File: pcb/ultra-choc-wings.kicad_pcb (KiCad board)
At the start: 2 copper layers, 103.7 x 91.1 mm, 84 parts, among them Q1 AO3400A, SW1 CPG1316S01D02_reversible, SW10 CPG1316S01D02_reversible, SW11 CPG1316S01D02_reversible, SW12 CPG1316S01D02_reversible, SW13 CPG1316S01D02_reversible, SW14 CPG1316S01D02_reversible, SW15 CPG1316S01D02_reversible, SW16 CPG1316S01D02_reversible, SW17 CPG1316S01D02_reversible, SW18 CPG1316S01D02_reversible, SW2 CPG1316S01D02_reversible, SW3 CPG1316S01D02_reversible, SW4 CPG1316S01D02_reversible, SW5 CPG1316S01D02_reversible, SW6 CPG1316S01D02_reversible, SW7 CPG1316S01D02_reversible, SW8 CPG1316S01D02_reversible, SW9 CPG1316S01D02_reversible

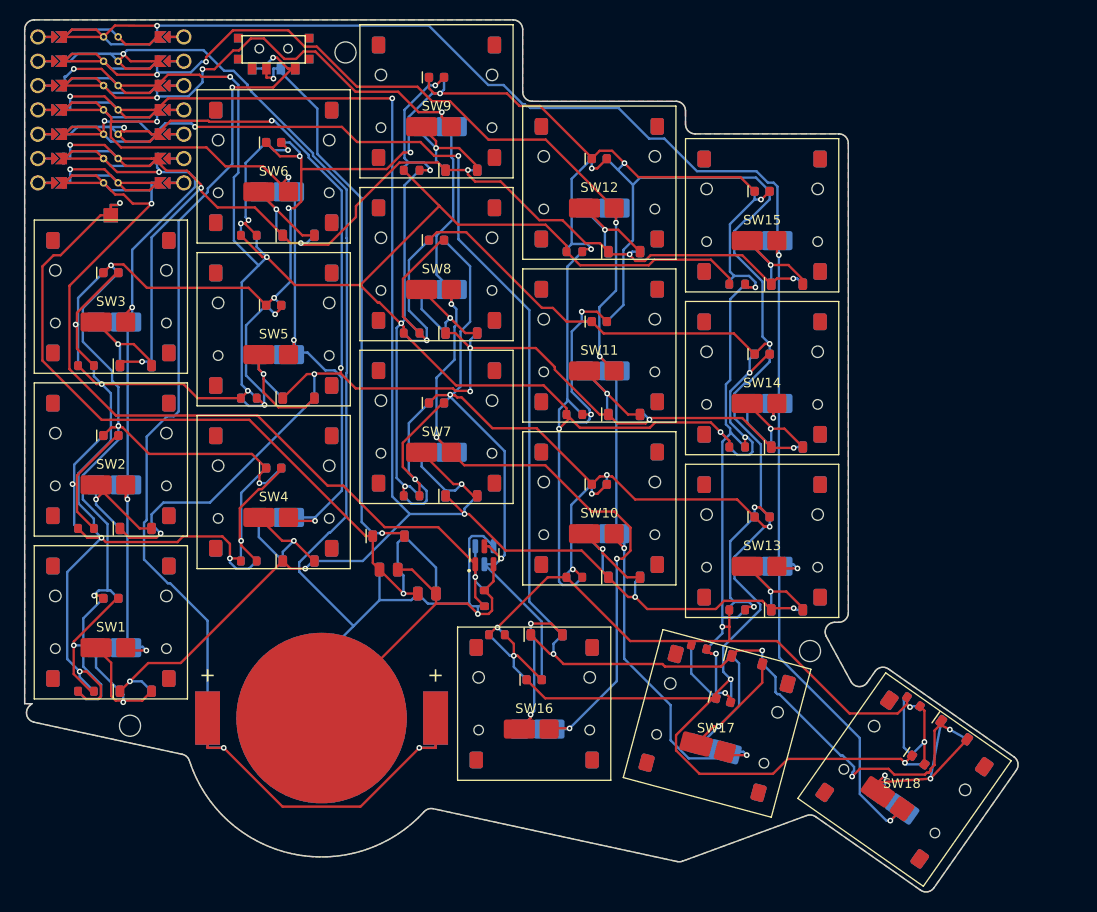
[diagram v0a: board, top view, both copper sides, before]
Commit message: Match the Chocofi key spacing, stagger and thumb cluster
Key centres now come straight from the Chocofi PCB (pashutk/chocofi):
18 x 17 mm pitch, column stagger 12 / 6 / -6.625 / -2.375 mm, thumbs at
fixed offsets from the bottom pinky key with a 0 / -15 / -30 degree fan.

The board top edge and power switch are now set from the pinky key so the
XIAO's top pin row stays on the board, and the thumb M2 hole moved off the
middle thumb diode. finish_routes.py reroutes tracks Freerouting leaves
inside the 0.3 mm edge rule, and the pour ties the XIAO's via-like GND
pads in solidly. Board rerouted, DRC has no new errors, gerbers, CPL and
case regenerated.

Co-Authored-By: Claude Opus 5.5 (1M context) <noreply@anthropic.com>
Claude-Session: https://claude.ai/code/session_01EJCFFVGKLmNFccuN3tJpCU
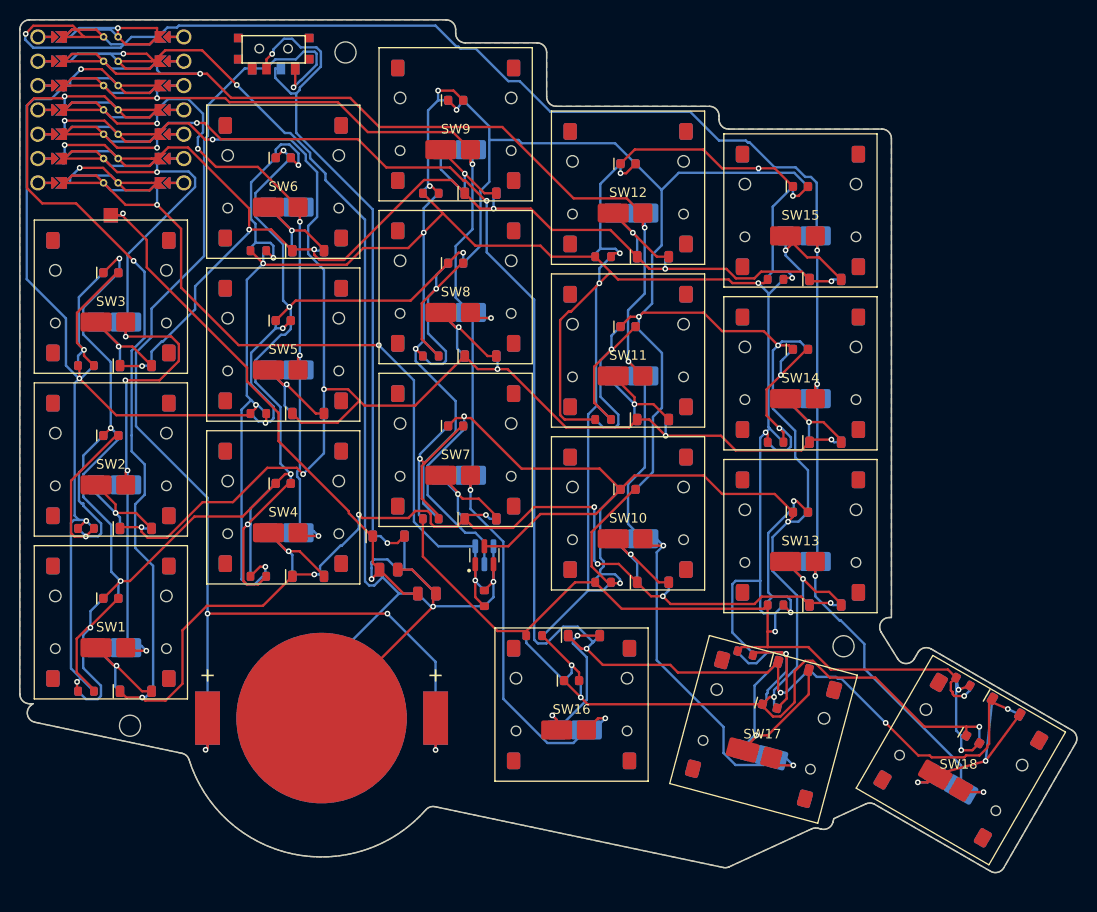
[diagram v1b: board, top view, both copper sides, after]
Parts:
- moved SW18 6.22 mm to (88.8, 14.4), turned to -30 degrees
- moved L18 6.09 mm to (90.0, 12.2), turned to -30 degrees
- moved D18 5.95 mm to (93.5, 8.80), turned to -30 degrees
- moved R18 5.57 mm to (89.0, 6.20), turned to -30 degrees
- moved D17 4.89 mm to (71.3, 4.56)
- moved L17 4.89 mm to (68.8, 8.77)
- moved SW17 4.89 mm to (68.2, 11.2)
- moved R17 4.89 mm to (66.2, 3.22)
- moved D13 4.03 mm to (74.6, -1.80)
- moved D14 4.03 mm to (74.6, -18.8)
- moved D15 4.03 mm to (74.6, -35.8)
- moved L13 4.03 mm to (72.0, -11.5)
- moved L14 4.03 mm to (72.0, -28.5)
- moved L15 4.03 mm to (72.0, -45.5)
- moved R13 4.03 mm to (69.4, -1.80)
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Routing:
- net LED_K: track 477.8 -> 456.3 mm, vias 17 -> 16
- net GND: track 166.7 -> 146.7 mm, vias 2 -> 4
- net P10: track 175.7 -> 193.8 mm, vias 7 -> 10
- net RAW: track 88.2 -> 70.8 mm
- net VCC3: track 451.3 -> 466.1 mm, vias 15 -> 14
- net P0: track 168.1 -> 182.1 mm
- net P2: track 143.3 -> 130.4 mm, vias 7 -> 5
- net LA_index_bottom: track 15.3 -> 27.5 mm, vias 2 -> 1
- net VCC5: track 0.00 -> 11.9 mm, vias 0 -> 1
- net SW_BAT: track 59.9 -> 71.6 mm
- net P6: track 94.1 -> 82.9 mm, vias 2 -> 3
- net P5: track 76.1 -> 86.0 mm, vias 4 -> 5
- net P3: track 85.4 -> 76.6 mm, vias 4 -> 5
- net P1: track 146.1 -> 154.5 mm, vias 6 -> 5
- net LA_middle_thumb: track 14.6 -> 22.3 mm, vias 2 -> 1
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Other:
- board size 103.7 x 91.1 mm -> 110.4 x 89 mm

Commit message: Re-route the board for the new outline
Full scripts/build_pcb.sh run: Freerouting, finish_routes, GND pours, DRC
(0 unconnected pads, nothing new versus master) and regenerated Gerbers.
BOM and CPL are unchanged.

Co-Authored-By: Claude Opus 5.5 (1M context) <noreply@anthropic.com>
Claude-Session: https://claude.ai/code/session_0165D9fBjcdWGjdLPuN9BjoD
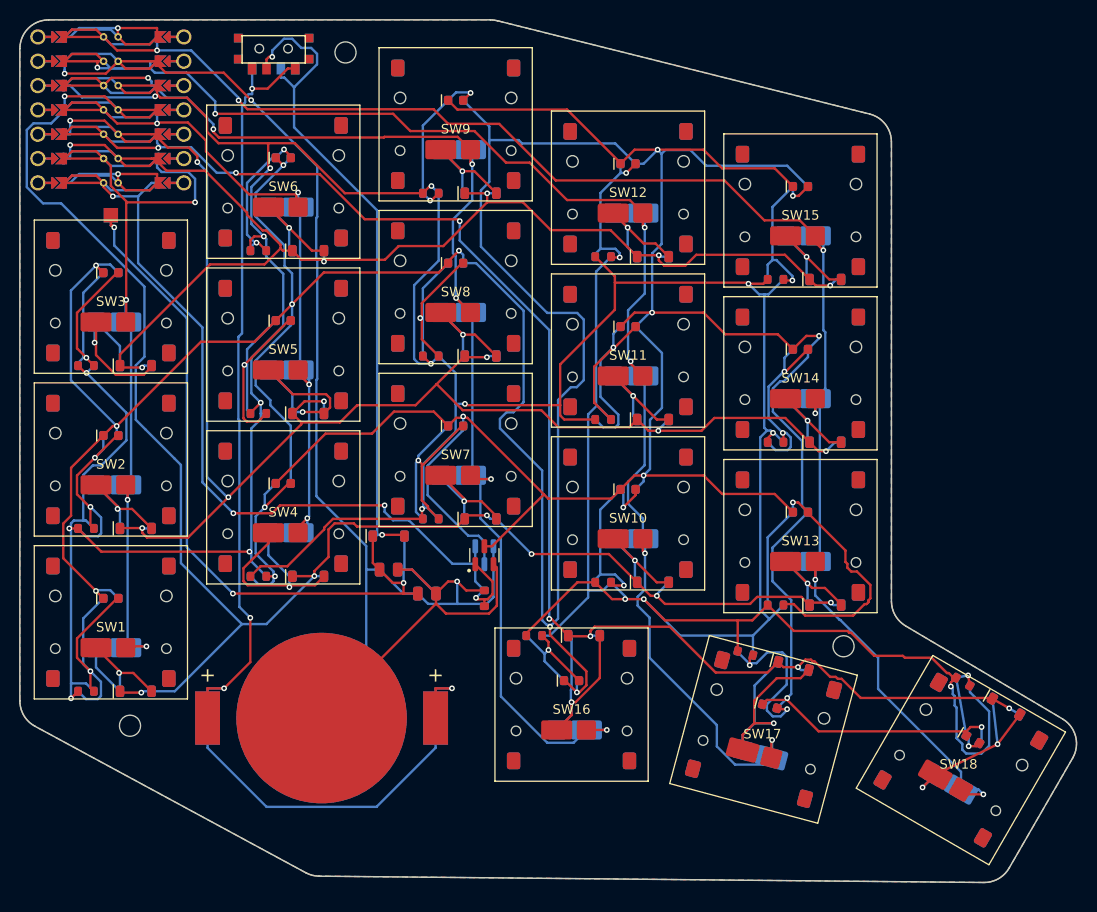
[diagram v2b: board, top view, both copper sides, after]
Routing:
- net LED_K: track 456.3 -> 563.1 mm, vias 16 -> 15
- net P4: track 170.1 -> 149.9 mm
- net P10: track 193.8 -> 174.5 mm, vias 10 -> 7
- net LA_inner_bottom: track 19.0 -> 36.3 mm, vias 2 -> 1
- net P0: track 182.1 -> 166.7 mm, vias 5 -> 6
- net RAW: track 70.8 -> 83.6 mm, vias 2 -> 3
- net GND: track 146.7 -> 158.3 mm, vias 4 -> 3
- net LA_pinky_home: track 30.5 -> 21.1 mm, vias 1 -> 2
- net VCC3: track 466.1 -> 475.1 mm, vias 14 -> 17
- net ring_bottom: track 13.4 -> 22.2 mm
- net BAT: track 135.7 -> 127.0 mm, vias 5 -> 4
- net LA_ring_home: track 18.2 -> 26.6 mm, vias 2 -> 1
- net LA_index_bottom: track 27.5 -> 19.8 mm, vias 1 -> 2
- net LA_ring_bottom: track 26.3 -> 19.5 mm, vias 1 -> 2
- net P6: track 82.9 -> 89.6 mm, vias 3 -> 4
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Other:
- board size 110.4 x 89 mm -> 110.3 x 90.1 mm
